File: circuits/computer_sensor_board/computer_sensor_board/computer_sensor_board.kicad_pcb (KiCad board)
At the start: 2 copper layers, 70 x 45 mm, 19 parts, among them J1 Conn_Switching_Hub, J2 Conn_Jetson, J5 Conn_VLP16, J6 Conn_Main_DCDC, J7 Conn_Router, Q2 2SJ555-E, U3 Heatsink_sheet

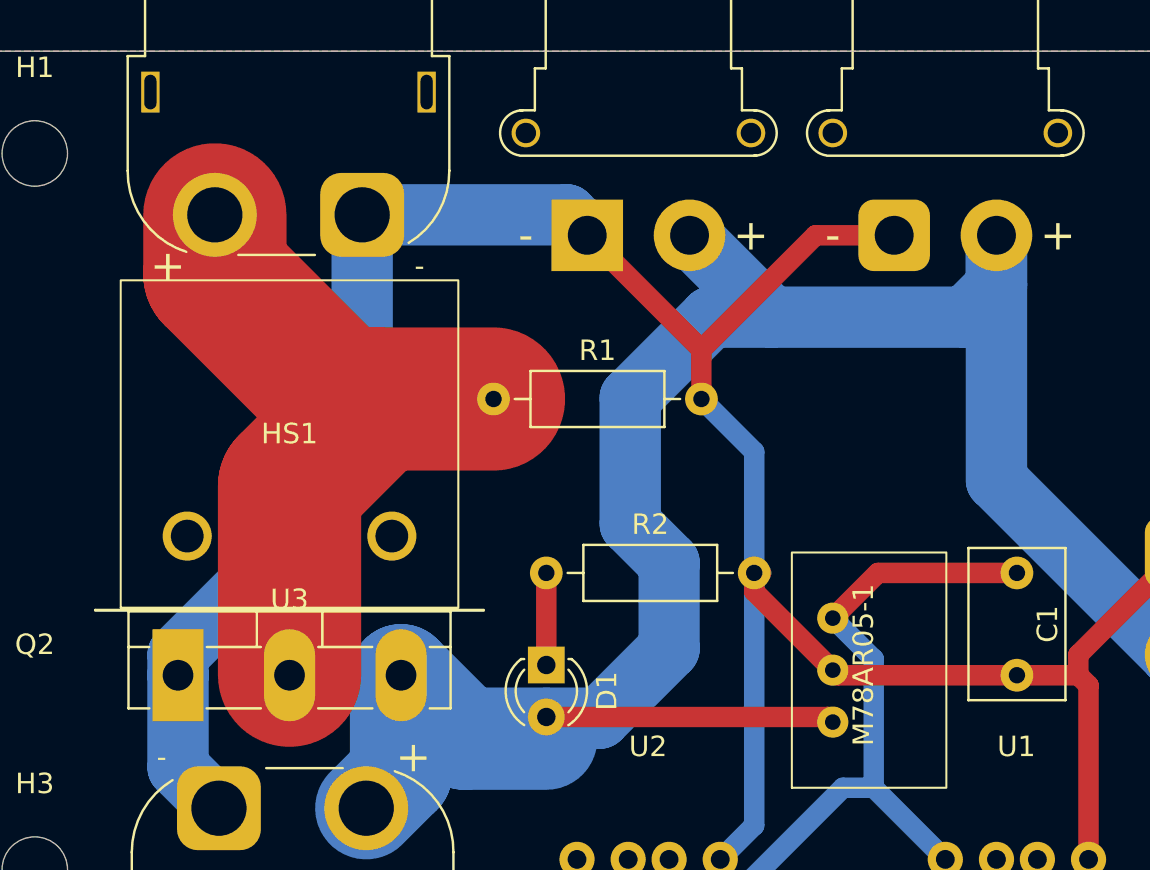
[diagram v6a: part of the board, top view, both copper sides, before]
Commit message: Fix/care invert connection (#379)
* add smart battery board

Signed-off-by: Masaya Kataoka <ms.kataoka@gmail.com>

* fix board design

Signed-off-by: Masaya Kataoka <ms.kataoka@gmail.com>

* change Pch MOSFET

Signed-off-by: Masaya Kataoka <ms.kataoka@gmail.com>

* add heatsink

Signed-off-by: Masaya Kataoka <ms.kataoka@gmail.com>

* remove warning

Signed-off-by: Masaya Kataoka <ms.kataoka@gmail.com>

* modify line

Signed-off-by: Masaya Kataoka <ms.kataoka@gmail.com>

* remove ERC violation

Signed-off-by: Masaya Kataoka <ms.kataoka@gmail.com>

---------

Signed-off-by: Masaya Kataoka <ms.kataoka@gmail.com>
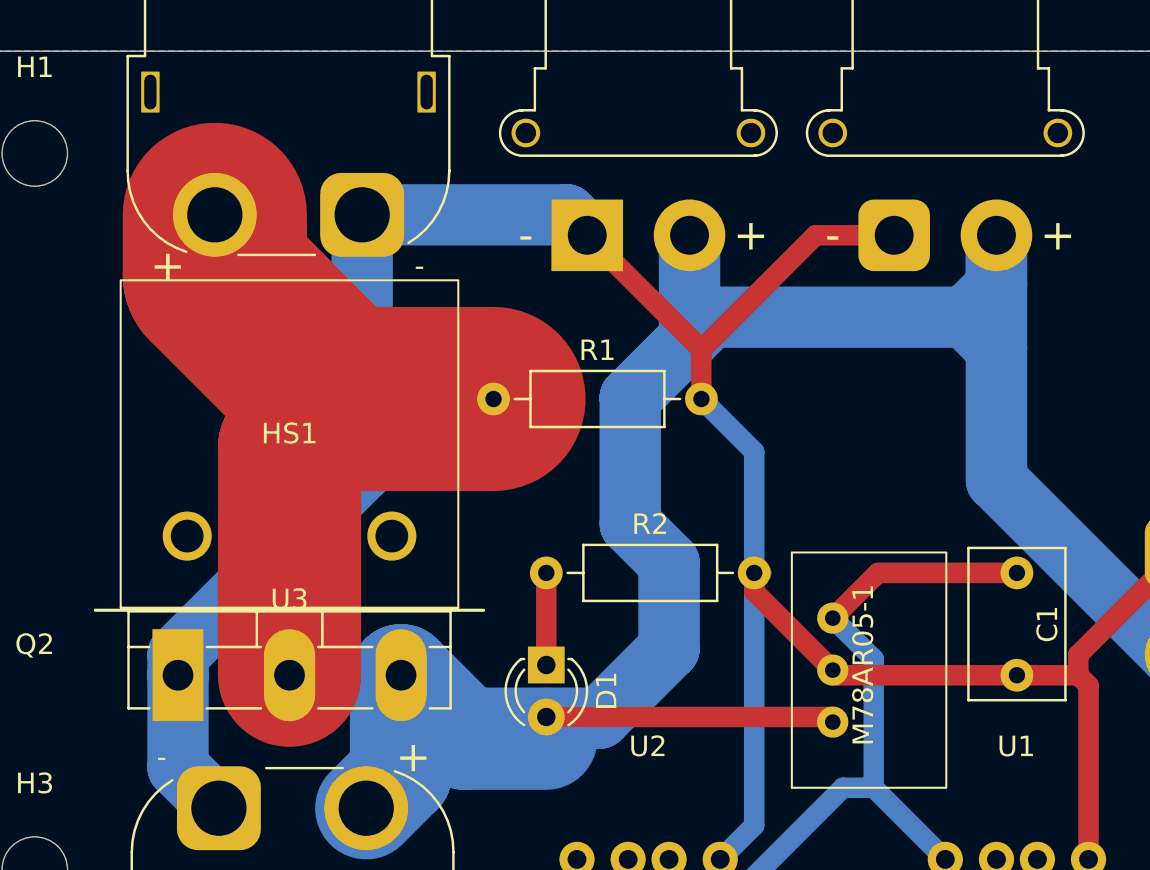
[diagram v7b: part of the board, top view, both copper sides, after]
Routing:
- net Net-(D1-A): track 102.9 -> 108.6 mm
- net Net-(J6-Pin_2): track 34.3 -> 33.6 mm
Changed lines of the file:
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@@
 	)
 	(segment
-		(start 191.7 62)
+		(start 189.846612 62)
 		(end 197.42 62)
-		(width 7)
+		(width 9)
 		(layer "F.Cu")
 		(net 7)
 	)
 	(segment
-		(start 189.900863 62)
-		(end 191.7 62)
-		(width 7)
-		(layer "F.Cu")
-		(net 7)
-	)
-	(segment
-		(start 183.8 55.899137)
-		(end 189.900863 62)
-		(width 7)
-		(layer "F.Cu")
-		(net 7)
-	)
-	(segment
-		(start 187.45 66.25)
-		(end 191.7 62)
+		(start 187.45 64.396612)
+		(end 189.846612 62)
 		(width 7)
 		(layer "F.Cu")
@@
 	(segment
 		(start 183.8 53)
-		(end 183.8 55.899137)
+		(end 183.8 55.953388)
+		(width 9)
+		(layer "F.Cu")
+		(net 7)
+	)
+	(segment
+		(start 187.45 75.5)
+		(end 187.45 64.396612)
 		(width 7)
 		(layer "F.Cu")
@@
 	)
 	(segment
-		(start 187.45 75.5)
-		(end 187.45 66.25)
-		(width 7)
+		(start 183.8 55.953388)
+		(end 189.846612 62)
+		(width 9)
 		(layer "F.Cu")
 		(net 7)
@@
 	)
 	(segment
-		(start 222 54)
-		(end 222 56.474873)
+		(start 222 59.5)
+		(end 221.974873 59.5)
 		(width 3)
 		(layer "B.Cu")
@@
 	)
 	(segment
-		(start 220.474873 58)
-		(end 211 58)
+		(start 208.044466 58)
+		(end 220.474873 58)
 		(width 3)
 		(layer "B.Cu")
@@
 		(start 202.6 77.6)
 		(end 200 77.6)
-		(width 3)
-		(layer "B.Cu")
-		(net 8)
-	)
-	(segment
-		(start 211 58)
-		(end 208.044466 58)
 		(width 3)
 		(layer "B.Cu")
@@
 	)
 	(segment
-		(start 222 65.964466)
+		(start 222 56.474873)
 		(end 222 54)
-		(width 3)
-		(layer "B.Cu")
-		(net 8)
-	)
-	(segment
-		(start 211 58)
-		(end 207 54)
-		(width 3)
-		(layer "B.Cu")
-		(net 8)
-	)
-	(segment
-		(start 222 56.474873)
-		(end 220.474873 58)
 		(width 3)
 		(layer "B.Cu")
@@
 	)
 	(segment
+		(start 204.1 61.944466)
+		(end 208.044466 58)
+		(width 3)
+		(layer "B.Cu")
+		(net 8)
+	)
+	(segment
 		(start 230.535534 74.5)
 		(end 231 74.5)
@@
 	)
 	(segment
-		(start 208.044466 58)
-		(end 204.1 61.944466)
+		(start 222 59.5)
+		(end 222 54)
 		(width 3)
 		(layer "B.Cu")
@@
 		(width 3)
 		(layer "B.Cu")
+		(net 8)
+	)
+	(segment
+		(start 207 59.044466)
+		(end 207 54)
+		(width 3)
+		(layer "B.Cu")
+		(net 8)
+	)
+	(segment
+		(start 220.474873 58)
+		(end 222 56.474873)
+		(width 3)
+		(layer "B.Cu")
+		(net 8)
+	)
+	(segment
+		(start 222 65.964466)
+		(end 222 59.5)
+		(width 3)
+		(layer "B.Cu")
+		(net 8)
+	)
+	(segment
+		(start 204.1 61.944466)
+		(end 207 59.044466)
+		(width 3)
+		(layer "B.Cu")
+		(net 8)
+	)
+	(segment
+		(start 221.974873 59.5)
+		(end 220.474873 58)
+		(width 3)
+		(layer "B.Cu")
